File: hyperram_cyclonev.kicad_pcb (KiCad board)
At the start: 2 copper layers, 90.1 x 89.7 mm, 57 parts, among them IC1 AP63205WU, IC2 TXB0108PWR, IC3 S26KL128SDABHI020, IC4 W25Q32JVSSIQ_TR, IC5 S27KL0641DABHI020, J1 ASP-122952-01, J2 HDMI_A, J3 1156915, J4 1156915, J5 Conn_02x06_Odd_Even, J6 Conn_02x06_Odd_Even, J7 Conn_02x06_Odd_Even, Q1 BSS138, Q2 BSS138

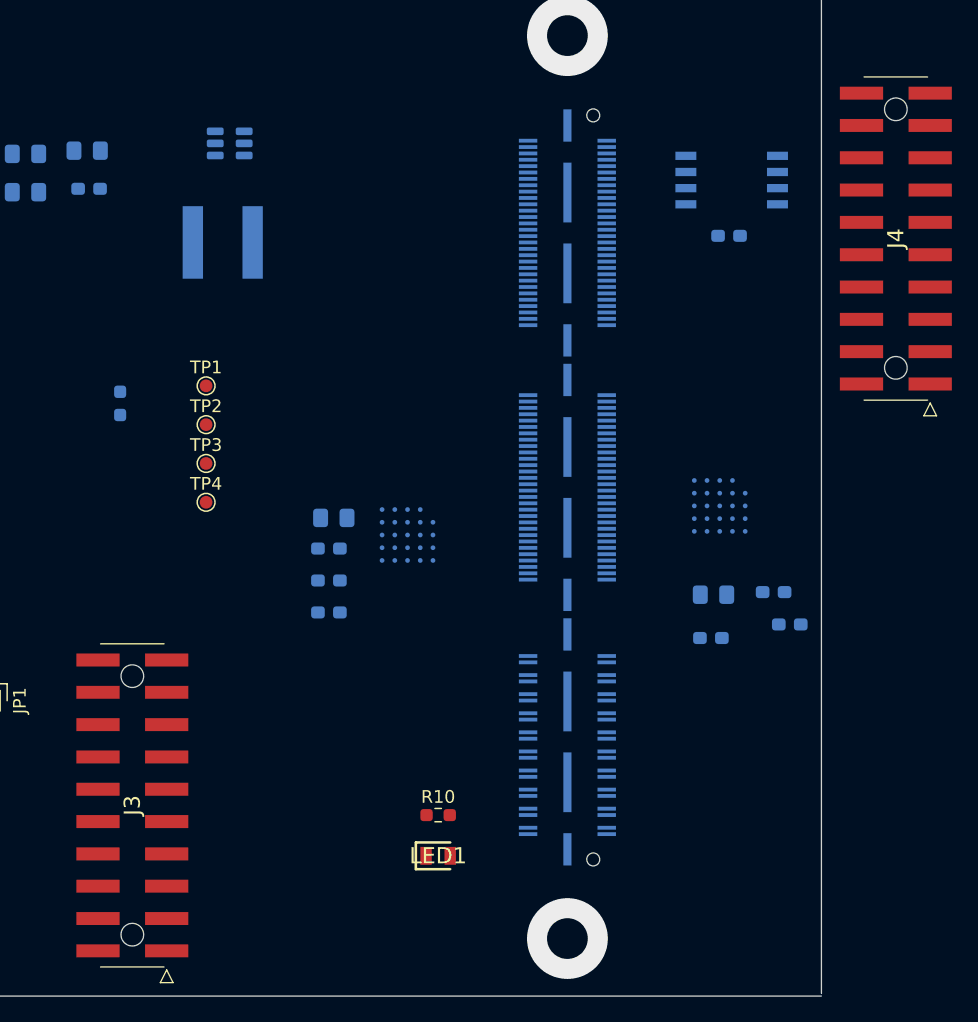
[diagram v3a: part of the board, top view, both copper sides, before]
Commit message: Changed two connectors from SMD to THT
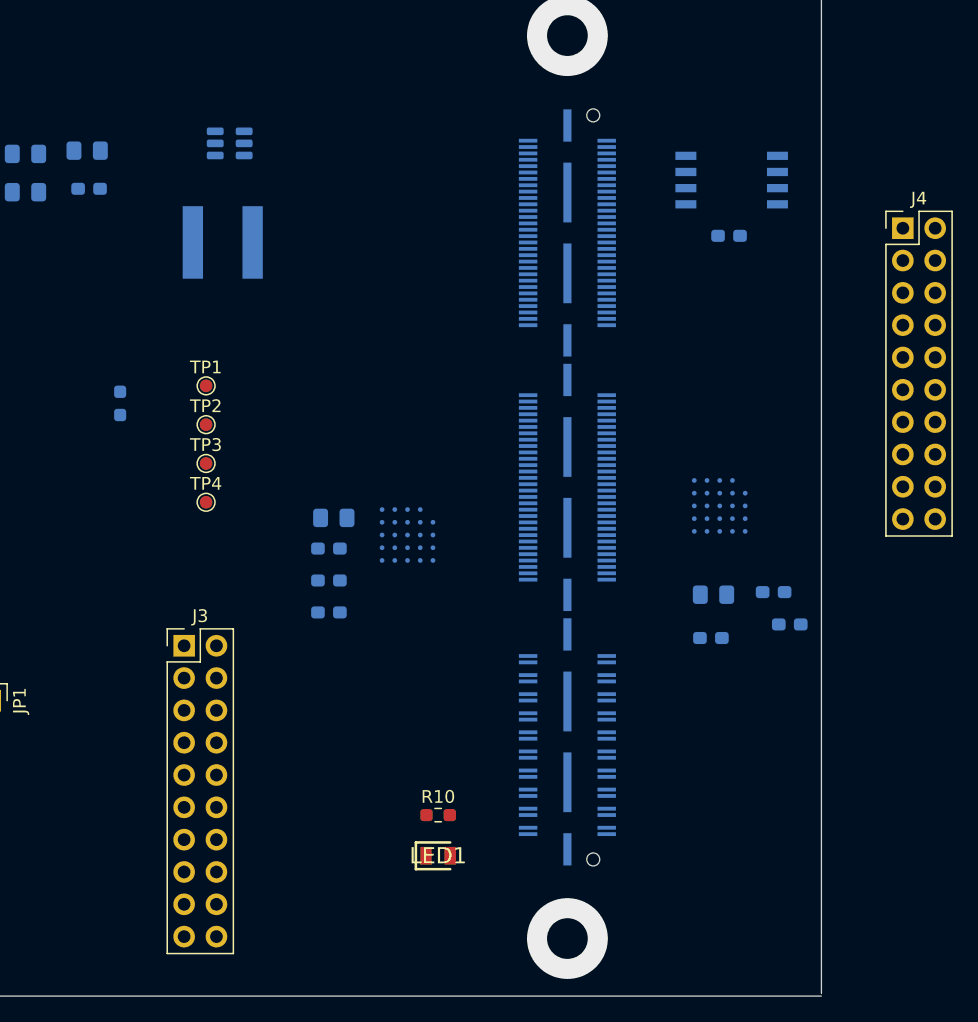
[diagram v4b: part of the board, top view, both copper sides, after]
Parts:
- J3, J4: value 1156915 -> Conn_02x10_Odd_Even; footprint hyperram_cyclonev:1156915 -> Connector_PinHeader_2.54mm:PinHeader_2x10_P2.54mm_Vertical
- moved J3 13.2 mm to (192.4, 125.6), turned to 0 degrees
- moved J4 0.98 mm to (248.9, 92.8), turned to 0 degrees
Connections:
- J3 pad 11: GND -> /pmod5lv_io3
- J3 pad 13: GND -> /pmod5lv_io2
- J3 pad 15: GND -> /pmod5lv_io1
- J3 pad 17: GND -> /pmod5lv_io0
- J3 pad 2: /pmod5lv_io0 -> GND
- J3 pad 3: /pmod5lv_io1 -> /pmod5lv_io7
- J3 pad 4: /pmod5lv_io2 -> GND
- J3 pad 5: /pmod5lv_io3 -> /pmod5lv_io6
- J3 pad 6: /pmod5lv_io4 -> GND
- J3 pad 8: /pmod5lv_io6 -> GND
- J3 pad 9: /pmod5lv_io7 -> /pmod5lv_io4
- J4 pad 11: GND -> /debug_io3
- J4 pad 12: /debug_io0 -> GND
- J4 pad 13: /debug_io1 -> /debug_io2
- J4 pad 14: /debug_io2 -> GND
- J4 pad 15: /debug_io3 -> /debug_io1
- J4 pad 16: /debug_io4 -> GND
- J4 pad 17: /debug_io5 -> /debug_io0
- J4 pad 18: /debug_io6 -> GND
- J4 pad 19: /debug_io7 -> GND
- J4 pad 3: GND -> /debug_io7
- J4 pad 5: GND -> /debug_io6
- J4 pad 7: GND -> /debug_io5
- J4 pad 9: GND -> /debug_io4

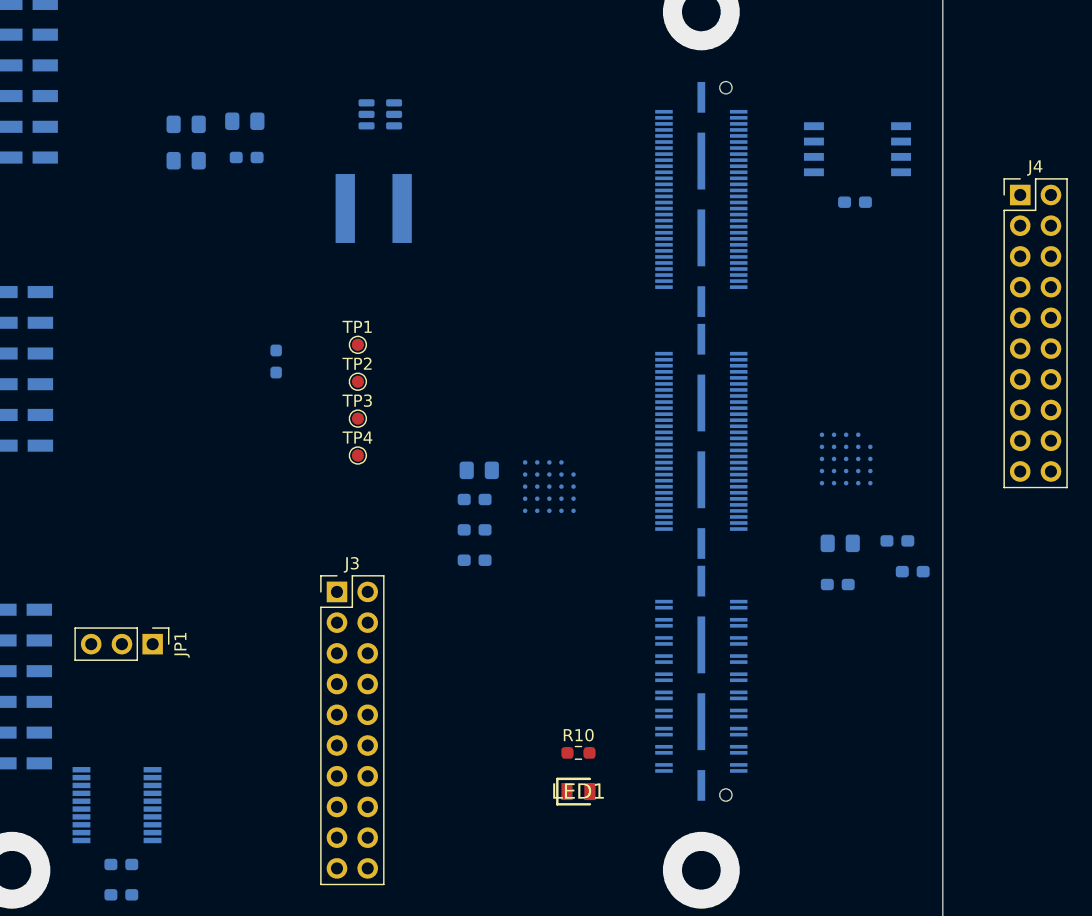
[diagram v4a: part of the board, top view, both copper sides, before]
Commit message: Rearrange signals assignments to simplify routing.
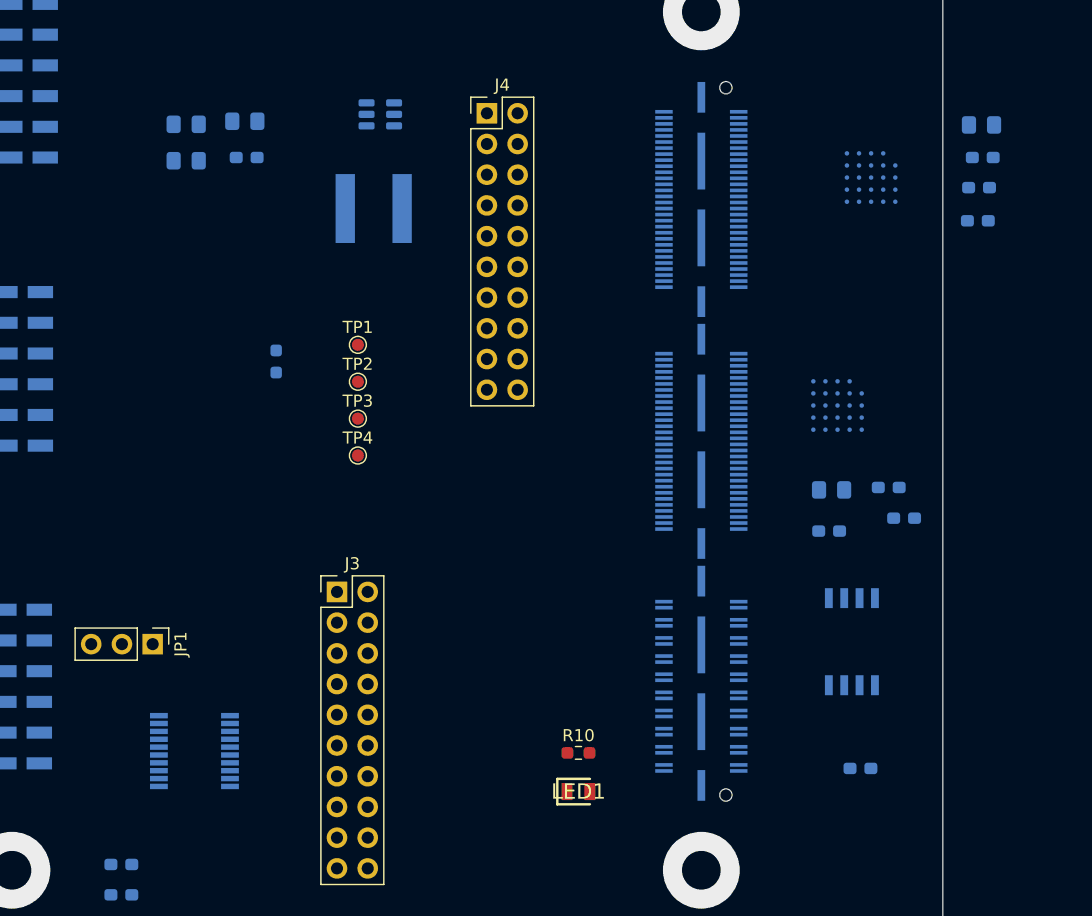
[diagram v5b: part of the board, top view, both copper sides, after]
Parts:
- moved C9 50.6 mm to (245.8, 89.7)
- moved C10 50.4 mm to (245.5, 92.2)
- moved C8 50.4 mm to (245.7, 87.0)
- moved C12 50.2 mm to (245.4, 94.9)
- moved C16 46.8 mm to (235.7, 140.2)
- moved J4 44.6 mm to (204.8, 86.1)
- moved IC4 40.7 mm to (234.9, 129.7), turned to -90 degrees
- moved IC3 36.9 mm to (236.5, 91.4)
- moved IC2 7.81 mm to (180.6, 138.8), turned to 180 degrees
- moved C13 4.48 mm to (233.1, 120.6)
- moved C15 4.48 mm to (239.3, 119.5)
- moved C11 4.48 mm to (233.3, 117.2)
- moved C14 4.48 mm to (238.0, 117.0)
- moved IC5 4.48 mm to (233.8, 110.2)
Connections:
- IC4 pad 7: /debug_io7 -> /flash_io3
- J1 pad 101: /debug_io3 -> /hpdet
- J1 pad 102: /pmod5lv_io6 -> /pmod3_io6p
- J1 pad 103: /debug_io4 -> /cec
- J1 pad 104: /pmod5lv_io7 -> /pmod3_io6n
- J1 pad 107: /debug_io5 -> /hr2_dq7
- J1 pad 108: /pmod3_io0p -> /pmod3_io7p
- J1 pad 109: /debug_io6 -> /hr2_dq6
- J1 pad 110: /pmod3_io0n -> /pmod3_io7n
- J1 pad 113: /debug_io7 -> /hr2_dq1
- J1 pad 114: /pmod3_io1p -> /debug_io0
- J1 pad 115: /flash_io2 -> /hr2_dq5
- J1 pad 116: /pmod3_io1n -> /debug_io1
- J1 pad 119: /flash_io1 -> /hr2_dq0
- J1 pad 120: /pmod3_io2p -> /debug_io2
- J1 pad 121: /flash_io0 -> /hr2_dq3
- J1 pad 122: /pmod3_io2n -> /debug_io3
- J1 pad 125: /flash_clk -> /hr2_dq4
- J1 pad 126: /pmod3_io3p -> /debug_io4
- J1 pad 127: /flash_csb -> /hr2_dq2
- J1 pad 128: /pmod3_io3n -> /debug_io5
- J1 pad 131: /hdmi_d2p -> /hf_psc
- J1 pad 132: /pmod3_io4p -> /ddc_dat_lv
- J1 pad 133: /hdmi_d2n -> /hf_pscn
- J1 pad 134: /pmod3_io4n -> /ddc_clk_lv
- J1 pad 137: /hdmi_d1p -> /hr2_rwds
- J1 pad 138: /pmod3_io5p -> /hdmi_d0p
- J1 pad 139: /hdmi_d1n -> /hf_csn
- J1 pad 140: /pmod3_io5n -> /hdmi_d0n
- J1 pad 143: /hdmi_d0p -> /hf_intn
- J1 pad 144: /pmod3_io6p -> /hdmi_d1p
- J1 pad 145: /hdmi_d0n -> /hr2_rstn
- J1 pad 146: /pmod3_io6n -> /hdmi_d1n
- J1 pad 149: /hdmi_clkp -> /hr2_csn
- J1 pad 150: /pmod3_io7p -> /hdmi_d2p
- J1 pad 151: /hdmi_clkn -> /hf_rston
- J1 pad 152: /pmod3_io7n -> /hdmi_d2n
- J1 pad 155: /ddc_dat_lv -> /hr2_clkp
- J1 pad 156: /hpdet -> /hdmi_clkp
- J1 pad 157: /ddc_clk_lv -> /hr2_clkn
- J1 pad 158: /cec -> /hdmi_clkn
- J1 pad 41: /hf_csn -> /flash_io3
- J1 pad 42: /hr2_csn -> /pmod5lv_io0
- J1 pad 43: /hr2_rstn -> /flash_clk
- J1 pad 44: /hr2_rwds -> /pmod5lv_io1
- J1 pad 47: /hf_rston -> /flash_io0
- J1 pad 48: /hr2_dq7 -> /pmod5lv_io2
- J1 pad 49: /hf_intn -> /flash_csb
- J1 pad 50: /hr2_dq6 -> /pmod5lv_io3
- J1 pad 53: /hr1_csn -> /flash_io1
- J1 pad 54: /hr2_dq5 -> /pmod5lv_io4
- J1 pad 55: /hr1_rwds -> /flash_io2
- J1 pad 56: /hr2_dq4 -> /pmod5lv_io5
- J1 pad 59: /hr1_dq7 -> /debug_io6
- J1 pad 60: /hr2_dq3 -> /pmod5lv_io6
- J1 pad 61: /hr1_dq6 -> /hr1_dq7
- J1 pad 62: /hr2_dq2 -> /pmod5lv_io7
- J1 pad 65: /hr1_dq5 -> /hr1_dq6
- J1 pad 66: /hr2_dq1 -> /pmod3_io0p
- J1 pad 67: /hr1_dq4 -> /hr1_dq1
- J1 pad 68: /hr2_dq0 -> /pmod3_io0n
- J1 pad 71: /hr1_dq3 -> /hr1_dq5
- J1 pad 72: /hr2_clkp -> /pmod3_io1p
- J1 pad 73: /hr1_dq2 -> /hr1_dq0
- J1 pad 74: /hr2_clkn -> /pmod3_io1n
- J1 pad 77: /hr1_dq1 -> /hr1_dq3
- J1 pad 78: /hf_psc -> /pmod3_io2p
- J1 pad 79: /hr1_dq0 -> /hr1_dq4
- J1 pad 80: /hf_pscn -> /pmod3_io2n
- J1 pad 83: /hr1_clkp -> /hr1_dq2
- J1 pad 84: /pmod5lv_io0 -> /pmod3_io3p
- J1 pad 85: /hr1_clkn -> /hr1_rwds
- J1 pad 86: /pmod5lv_io1 -> /pmod3_io3n
- J1 pad 90: /pmod5lv_io2 -> /pmod3_io4p
- J1 pad 91: /debug_io0 -> /hr1_csn
- J1 pad 92: /pmod5lv_io3 -> /pmod3_io4n
- J1 pad 95: /debug_io1 -> /hr1_clkp
- J1 pad 96: /pmod5lv_io4 -> /pmod3_io5p
- J1 pad 97: /debug_io2 -> /hr1_clkn
- J1 pad 98: /pmod5lv_io5 -> /pmod3_io5n
- J4 pad 3: /debug_io7 -> /cec

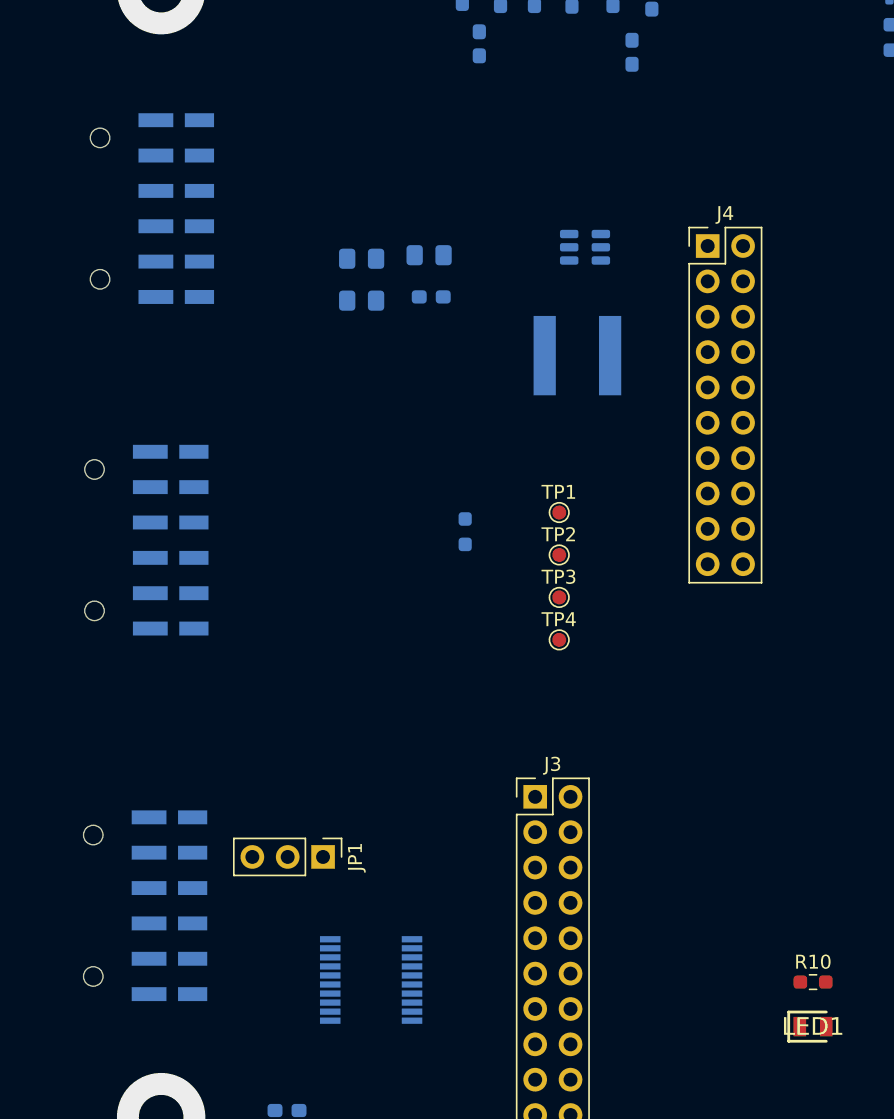
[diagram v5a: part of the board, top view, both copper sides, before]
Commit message: Reaarranged signals assignments to simplify routing
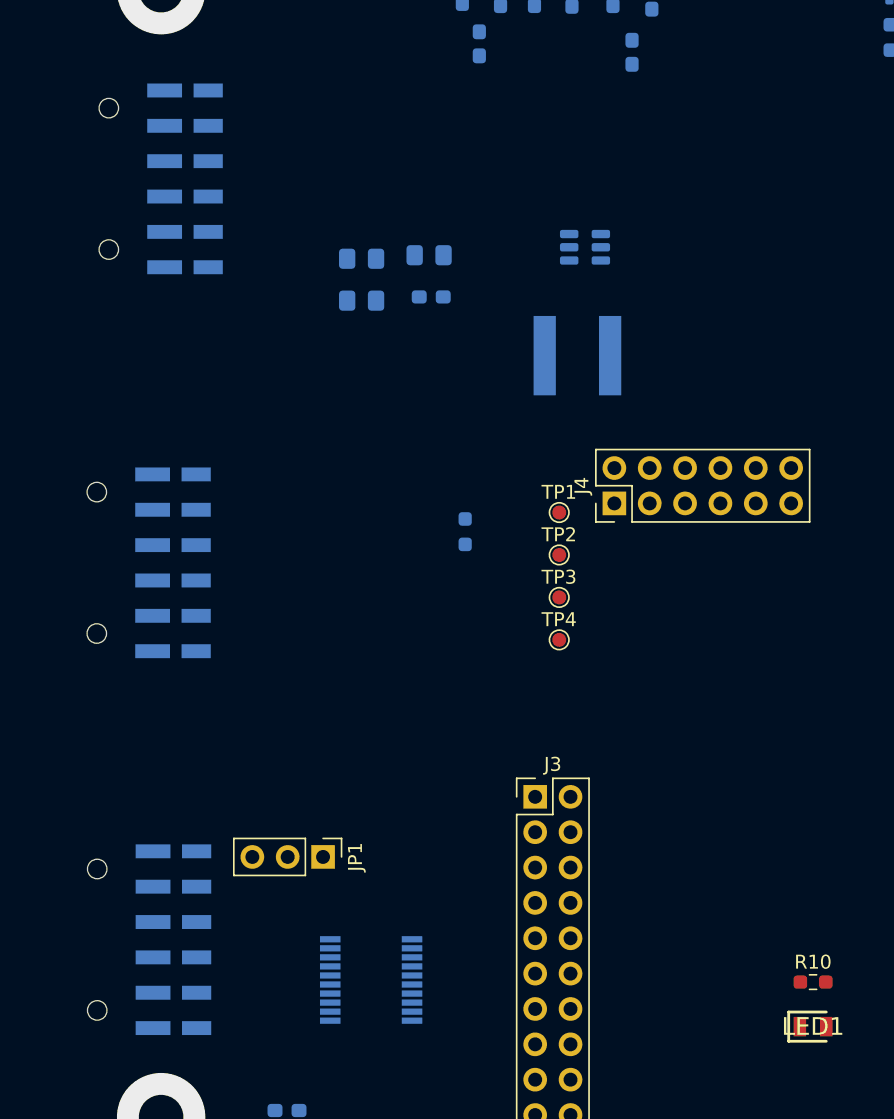
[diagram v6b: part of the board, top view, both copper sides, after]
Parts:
- J4: value Conn_02x10_Odd_Even -> Conn_02x06_Odd_Even; footprint Connector_PinHeader_2.54mm:PinHeader_2x10_P2.54mm_Vertical -> Connector_PinHeader_2.54mm:PinHeader_2x06_P2.54mm_Vertical
- J5, J6, J7: value Conn_02x06_Odd_Even -> Conn_02x06_Top_Bottom; footprint hyperram_cyclonev:610112249221 -> hyperram_cyclonev:610112249221_PMOD_Bottom
- moved J4 19.7 mm to (198.1, 104.5), turned to 90 degrees
- moved J5 2.46 mm to (161.0, 135.9)
- moved J7 2.23 mm to (161.8, 81.2)
- moved J6 1.63 mm to (161.0, 108.8)
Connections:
- IC2 pad 1: /pmod5lv_io0 -> /pmod5lv_io7
- IC2 pad 12: /pmod5_io7 -> /pmod5_io0
- IC2 pad 13: /pmod5_io6 -> /pmod5_io1
- IC2 pad 14: /pmod5_io5 -> /pmod5_io2
- IC2 pad 15: /pmod5_io4 -> /pmod5_io3
- IC2 pad 16: /pmod5_io3 -> /pmod5_io4
- IC2 pad 17: /pmod5_io2 -> /pmod5_io5
- IC2 pad 18: /pmod5_io1 -> /pmod5_io6
- IC2 pad 20: /pmod5_io0 -> /pmod5_io7
- IC2 pad 3: /pmod5lv_io1 -> /pmod5lv_io6
- IC2 pad 4: /pmod5lv_io2 -> /pmod5lv_io5
- IC2 pad 5: /pmod5lv_io3 -> /pmod5lv_io4
- IC2 pad 6: /pmod5lv_io4 -> /pmod5lv_io3
- IC2 pad 7: /pmod5lv_io5 -> /pmod5lv_io2
- IC2 pad 8: /pmod5lv_io6 -> /pmod5lv_io1
- IC2 pad 9: /pmod5lv_io7 -> /pmod5lv_io0
- J1 pad 102: /pmod3_io6p -> /debug_io2
- J1 pad 104: /pmod3_io6n -> /debug_io1
- J1 pad 108: /pmod3_io7p -> /pmod3_io4p
- J1 pad 110: /pmod3_io7n -> /pmod3_io4n
- J1 pad 114: /debug_io0 -> /pmod3_io5p
- J1 pad 116: /debug_io1 -> /pmod3_io5n
- J1 pad 120: /debug_io2 -> /pmod3_io6p
- J1 pad 122: /debug_io3 -> /pmod3_io6n
- J1 pad 126: /debug_io4 -> /pmod3_io7p
- J1 pad 128: /debug_io5 -> /pmod3_io7n
- J1 pad 59: /debug_io6 -> /debug_io7
- J1 pad 90: /pmod3_io4p -> /debug_io6
- J1 pad 92: /pmod3_io4n -> /debug_io5
- J1 pad 96: /pmod3_io5p -> /debug_io4
- J1 pad 98: /pmod3_io5n -> /debug_io3
- J4 pad 1: GND -> /cec
- J4 pad 11: /debug_io3 -> +3V3
- J4 pad 12: GND -> +3V3
- J4 pad 2: GND -> /debug_io1
- J4 pad 3: /cec -> /debug_io2
- J4 pad 4: GND -> /debug_io3
- J4 pad 5: /debug_io6 -> /debug_io4
- J4 pad 6: GND -> /debug_io5
- J4 pad 7: /debug_io5 -> /debug_io6
- J4 pad 8: GND -> /debug_io7
- J4 pad 9: /debug_io4 -> GND
- J5 pad 1: /pmod5_io6 -> /pmod5_io0
- J5 pad 10: GND -> /pmod5_io7
- J5 pad 11: VCCQ -> GND
- J5 pad 2: /pmod5_io7 -> /pmod5_io2
- J5 pad 4: /pmod5_io5 -> /pmod5_io6
- J5 pad 5: /pmod5_io2 -> GND
- J5 pad 6: /pmod5_io3 -> VCCQ
- J5 pad 7: /pmod5_io0 -> /pmod5_io1
- J5 pad 8: /pmod5_io1 -> /pmod5_io3
- J5 pad 9: GND -> /pmod5_io5
- J6 pad 1: /pmod3_io3n -> /pmod3_io0n
- J6 pad 10: GND -> /pmod3_io3p
- J6 pad 11: +3V3 -> GND
- J6 pad 2: /pmod3_io3p -> /pmod3_io1n
- J6 pad 4: /pmod3_io2p -> /pmod3_io3n
- J6 pad 5: /pmod3_io1n -> GND
- J6 pad 6: /pmod3_io1p -> +3V3
- J6 pad 7: /pmod3_io0n -> /pmod3_io0p
- J6 pad 8: /pmod3_io0p -> /pmod3_io1p
- J6 pad 9: GND -> /pmod3_io2p
- J7 pad 1: /pmod3_io7n -> /pmod3_io4n
- J7 pad 10: GND -> /pmod3_io7p
- J7 pad 11: +3V3 -> GND
- J7 pad 2: /pmod3_io7p -> /pmod3_io5n
- J7 pad 4: /pmod3_io6p -> /pmod3_io7n
- J7 pad 5: /pmod3_io5n -> GND
- J7 pad 6: /pmod3_io5p -> +3V3
- J7 pad 7: /pmod3_io4n -> /pmod3_io4p
- J7 pad 8: /pmod3_io4p -> /pmod3_io5p
- J7 pad 9: GND -> /pmod3_io6p
